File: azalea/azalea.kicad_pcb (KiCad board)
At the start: 4 copper layers, 70.6 x 53.3 mm, 103 parts, among them J1 NEIGHBOR1, J2 NEIGHBOR2, J3 USB-MICRO-B-SHIELDED, J4 USB-MICRO-B-SHIELDED, J5 JTAG, J6 POWER, J7 BONUS_ROW, SW1 DFU, SW2 RESET, U1 LPC4330FBD144, U2 W25Q16DV, U3 AP7333, U4 IP4220CZ6, U5 AP2553W6-7, X1 MCU_XTAL, X2 RTC_XTAL

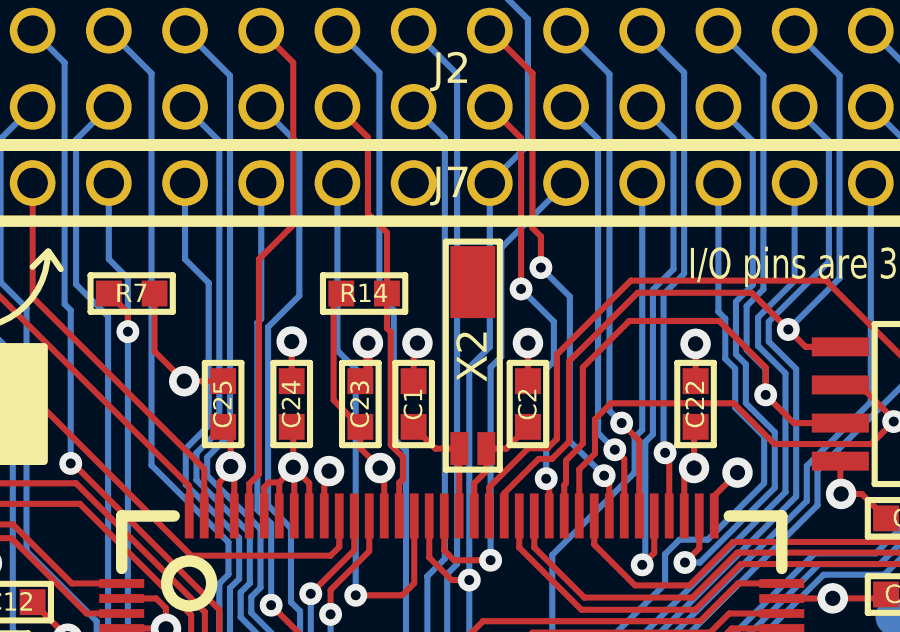
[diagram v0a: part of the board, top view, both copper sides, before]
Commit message: Azalea: changed J7 pin 10 from GND to RTCX1
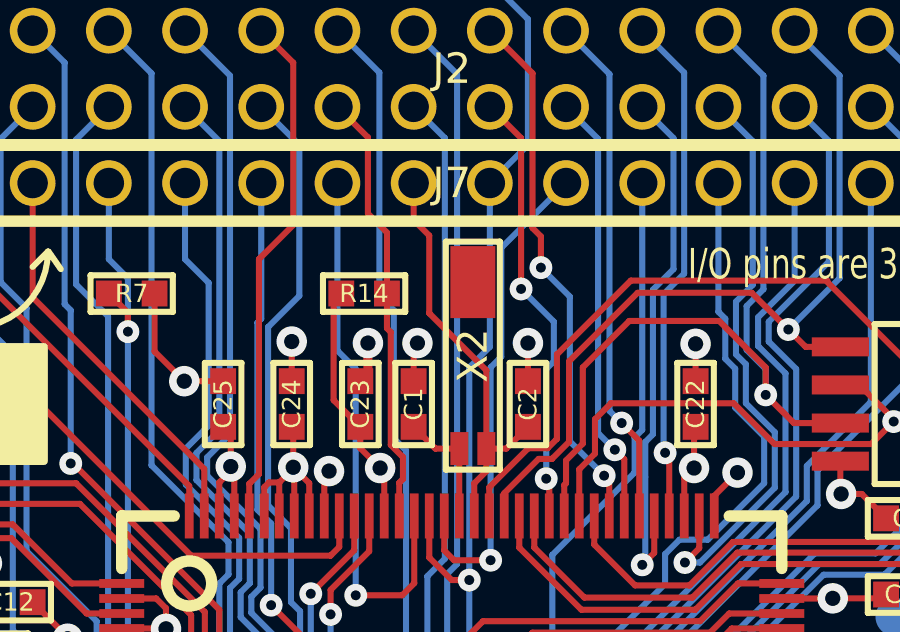
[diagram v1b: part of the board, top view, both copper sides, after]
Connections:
- J7 pad 10: GND -> /RTCX1
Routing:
- net /RTCX1: track 4.10 -> 14.0 mm
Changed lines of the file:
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@@
     (links 387)
     (no_connects 0)
-    (area 105.842999 71.044999 176.605001 124.535001)
+    (area 93.424104 68.58 207.466001 127.000001)
     (thickness 1.6)
     (drawings 311)
-    (tracks 1583)
+    (tracks 1588)
     (zones 0)
     (modules 103)
@@
     (company "Copyright 2015-2018 Great Scott Gadgets")
     (comment 1 "License: BSD-3-Clause")
-    (comment 2 http://greatscottgadgets.com/greatfet/)
+    (comment 2 https://greatscottgadgets.com/greatfet/)
   )
   (layers
@@
       (net 102 /RTC_ALARM))
     (pad 10 thru_hole circle (at -1.27 0) (size 1.524 1.524) (drill 1.016) (layers *.Cu *.Mask F.SilkS)
-      (net 1 GND))
+      (net 2 /RTCX1))
     (pad 11 thru_hole circle (at 1.27 0) (size 1.524 1.524) (drill 1.016) (layers *.Cu *.Mask F.SilkS)
       (net 100 /RESET))
@@
   (segment (start 144.526 116.332) (end 145.796 116.332) (width 0.2032) (layer F.Cu) (net 1) (status 10))
   (via (at 145.796 116.332) (size 1.016) (drill 0.508) (layers F.Cu B.Cu) (net 1))
+  (segment (start 143.394 87.592) (end 143.394 84.984) (width 0.2032) (layer F.Cu) (net 2))
+  (segment (start 140.97 79.97) (end 140.97 78.74) (width 0.2032) (layer F.Cu) (net 2))
+  (segment (start 141.49 80.49) (end 140.97 79.97) (width 0.2032) (layer F.Cu) (net 2))
+  (segment (start 141.49 83.08) (end 141.49 80.49) (width 0.2032) (layer F.Cu) (net 2))
+  (segment (start 143.394 84.984) (end 141.49 83.08) (width 0.2032) (layer F.Cu) (net 2))
   (segment (start 144.78 86.868) (end 144.056 87.592) (width 0.2032) (layer F.Cu) (net 2) (status 10))
   (segment (start 144.056 87.592) (end 143.394 87.592) (width 0.2032) (layer F.Cu) (net 2) (status 20))
